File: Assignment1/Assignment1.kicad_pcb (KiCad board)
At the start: 2 copper layers, 50 x 50 mm, 22 parts, among them J1 Conn_01x02_Pin, J2 Conn_01x02_Pin, U1 TPS51386RJNR

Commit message: as1: momoi silkscreen and update bom
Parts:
- added G***: LOGO, momoi-n.preety:momoi-n, F.Cu at (58.5, 92.0)
- moved C8 13.5 mm to (89.5, 85.5)
- moved C3 9.00 mm to (80.5, 85.5)
- moved C2 4.50 mm to (76.0, 85.5)
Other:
- board text added: "NI__"
- board text added: "PCB Design Assignment 1"
- board text added: "Two-Stage Voltage Converter"

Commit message: add vias and copper zone as solid
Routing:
- net Earth: vias 8 -> 303
- added copper zone on F.Cu, net /Buck_SW

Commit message: Add silk screen for Vin, Vout and update track angle to 45
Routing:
- net /Buck_VBST: track 6.90 -> 6.32 mm
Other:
- board text added: "Vin"
- board text added: "Vout"
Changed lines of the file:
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@@
 		(layer "Edge.Cuts")
+	)
+	(gr_text "Vout\n"
+		(at 56.5 57 0)
+		(layer "F.Paste")
+		(effects
+			(font
+				(size 1 1)
+				(thickness 0.15)
+			)
+			(justify left bottom)
+		)
+	)
+	(gr_text "Vin"
+		(at 95 57.5 0)
+		(layer "F.Paste")
+		(effects
+			(font
+				(size 1 1)
+				(thickness 0.15)
+			)
+			(justify left bottom)
+		)
 	)
 	(gr_text "Two-Stage Voltage Converter"
@@
 	)
 	(segment
-		(start 94.525 76.975)
+		(start 94.525 75.975)
 		(end 94.525 75)
-		(width 0.3)
+		(width 0.35)
+		(layer "F.Cu")
+		(net 9)
+	)
+	(segment
+		(start 90.5 77)
+		(end 93.5 77)
+		(width 0.35)
 		(layer "F.Cu")
 		(net 9)
@@
 	)
 	(segment
-		(start 94.5 77)
-		(end 94.525 76.975)
-		(width 0.3)
+		(start 93.5 77)
+		(end 94.525 75.975)
+		(width 0.35)
 		(layer "F.Cu")
 		(net 9)
-	)
-	(segment
-		(start 90.5 77)
-		(end 94.5 77)
-		(width 0.3)
-		(layer "F.Cu")
-		(net 9)

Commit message: R1 C1 route
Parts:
- moved R1 2.17 mm to (94.5, 77.0)
- moved C1 1.28 mm to (94.5, 79.0)
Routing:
- net /Buck_VBST: track 6.32 -> 3.77 mm
- net Net-(C1-Pad1): track 4.16 -> 2.02 mm
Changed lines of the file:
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@@
 	(footprint "Capacitor_SMD:C_0603_1608Metric"
 		(layer "F.Cu")
-		(at 95.775 79 180)
+		(at 94.5 79 180)
 		(descr "Capacitor SMD 0603 (1608 Metric), square (rectangular) end terminal, IPC_7351 nominal, (Body size source: IPC-SM-782 page 76, https://www.pcb-3d.com/wordpress/wp-content/uploads/ipc-sm-782a_amendment_1_and_2.pdf), generated with kicad-footprint-generator")
 		(tags "capacitor")
@@
 	(footprint "Resistor_SMD:R_0603_1608Metric"
 		(layer "F.Cu")
-		(at 95.35 75)
+		(at 94.5 77)
 		(descr "Resistor SMD 0603 (1608 Metric), square (rectangular) end terminal, IPC_7351 nominal, (Body size source: IPC-SM-782 page 72, https://www.pcb-3d.com/wordpress/wp-content/uploads/ipc-sm-782a_amendment_1_and_2.pdf), generated with kicad-footprint-generator")
 		(tags "resistor")
@@
 	)
 	(segment
-		(start 96.55 75.55)
-		(end 96.55 79)
-		(width 0.3)
+		(start 95.325 78.95)
+		(end 95.275 79)
+		(width 1)
 		(layer "F.Cu")
 		(net 1)
 	)
 	(segment
-		(start 96.175 75)
-		(end 96.175 75.175)
-		(width 0.3)
+		(start 95.325 77)
+		(end 95.325 78.95)
+		(width 1)
 		(layer "F.Cu")
 		(net 1)
 	)
 	(segment
-		(start 96.175 75.175)
-		(end 96.55 75.55)
-		(width 0.3)
+		(start 93.725 79)
+		(end 92.5 79)
+		(width 1)
 		(layer "F.Cu")
-		(net 1)
+		(net 2)
 	)
 	(segment
@@
 	)
 	(segment
-		(start 93 78.5)
-		(end 90.5 78.5)
-		(width 0.3)
+		(start 92.5 79)
+		(end 92 78.5)
+		(width 1)
+		(layer "F.Cu")
+		(net 2)
+	)
+	(segment
+		(start 92 78.5)
+		(end 89.675 78.5)
+		(width 1)
 		(layer "F.Cu")
 		(net 2)
@@
 	)
 	(segment
-		(start 93.5 79)
-		(end 93 78.5)
-		(width 0.3)
-		(layer "F.Cu")
-		(net 2)
-	)
-	(segment
 		(start 89.875 77)
 		(end 89.875 75.775)
@@
 	)
 	(segment
-		(start 95 79)
-		(end 93.5 79)
-		(width 0.3)
-		(layer "F.Cu")
-		(net 2)
-	)
-	(segment
 		(start 90.5 73.5)
 		(end 90.4 73.6)
@@
 	)
 	(segment
+		(start 91.45 76.15)
+		(end 91.3 76)
+		(width 0.3)
+		(layer "F.Cu")
+		(net 7)
+	)
+	(segment
 		(start 94.675 71.5)
 		(end 94.675 70.325)
@@
 	)
 	(segment
-		(start 93.5 76)
-		(end 93.35 76.15)
+		(start 94.675 72.325)
+		(end 93.5 73.5)
 		(width 0.3)
 		(layer "F.Cu")
@@
 	)
 	(segment
-		(start 94.675 72.325)
-		(end 93.5 73.5)
+		(start 93.5 73.5)
+		(end 93.5 75.5)
 		(width 0.3)
 		(layer "F.Cu")
@@
 	)
 	(segment
-		(start 93.5 73.5)
-		(end 93.5 76)
+		(start 92.85 76.15)
+		(end 91.45 76.15)
 		(width 0.3)
 		(layer "F.Cu")
@@
 	)
 	(segment
-		(start 93.35 76.15)
-		(end 91.45 76.15)
-		(width 0.3)
-		(layer "F.Cu")
-		(net 7)
-	)
-	(segment
-		(start 91.45 76.15)
-		(end 91.3 76)
+		(start 93.5 75.5)
+		(end 92.85 76.15)
 		(width 0.3)
 		(layer "F.Cu")
@@
 	)
 	(segment
-		(start 90.4 76.9)
-		(end 90.5 77)
-		(width 0.3)
+		(start 91 77)
+		(end 93.675 77)
+		(width 0.5)
 		(layer "F.Cu")
 		(net 9)
 	)
 	(segment
-		(start 94.525 75.975)
-		(end 94.525 75)
-		(width 0.35)
+		(start 90.4 76.15)
+		(end 90.4 76.4)
+		(width 0.3)
 		(layer "F.Cu")
 		(net 9)
 	)
 	(segment
-		(start 90.5 77)
-		(end 93.5 77)
-		(width 0.35)
+		(start 90.5 76.5)
+		(end 91 77)
+		(width 0.5)
 		(layer "F.Cu")
 		(net 9)
 	)
 	(segment
-		(start 90.4 76.15)
-		(end 90.4 76.9)
+		(start 90.4 76.4)
+		(end 90.5 76.5)
 		(width 0.3)
 		(layer "F.Cu")
 		(net 9)
-	)
-	(segment
-		(start 93.5 77)
-		(end 94.525 75.975)
-		(width 0.35)
-		(layer "F.Cu")
-		(net 9)

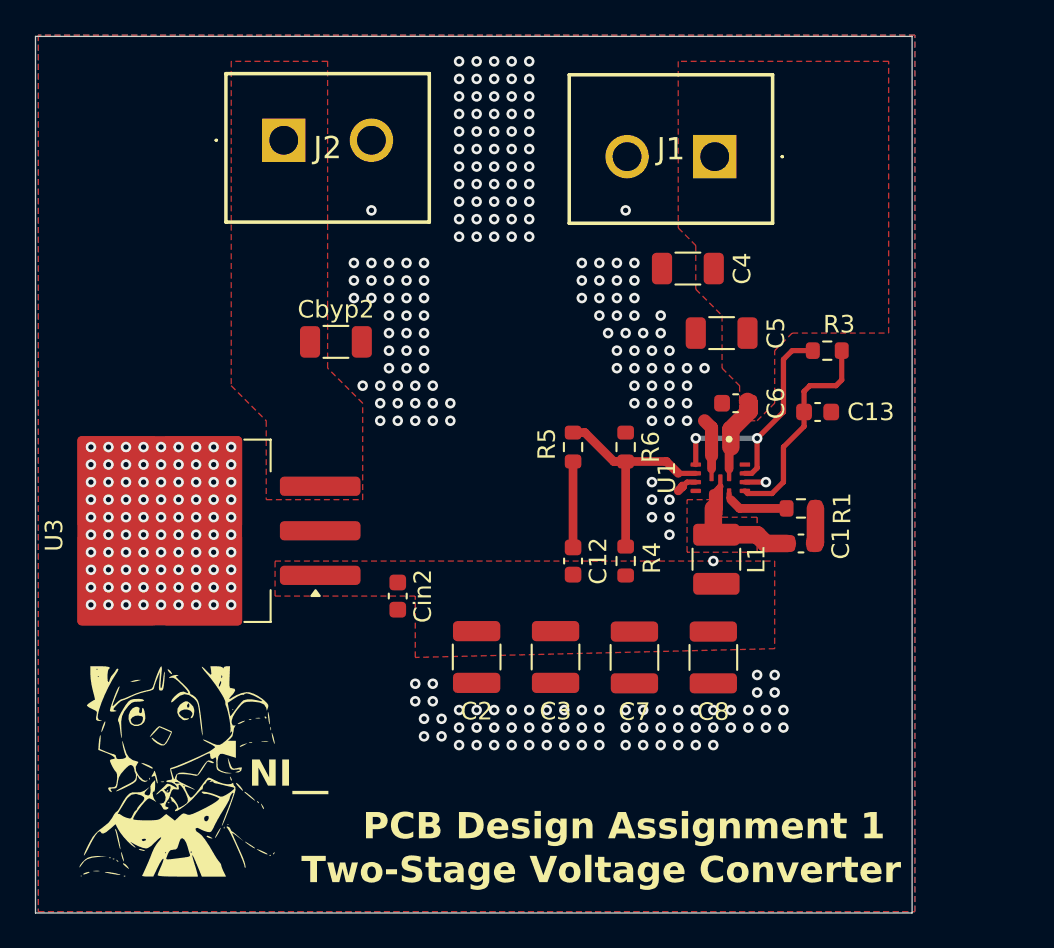
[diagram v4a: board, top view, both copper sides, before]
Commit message: make LDO copper plane solid
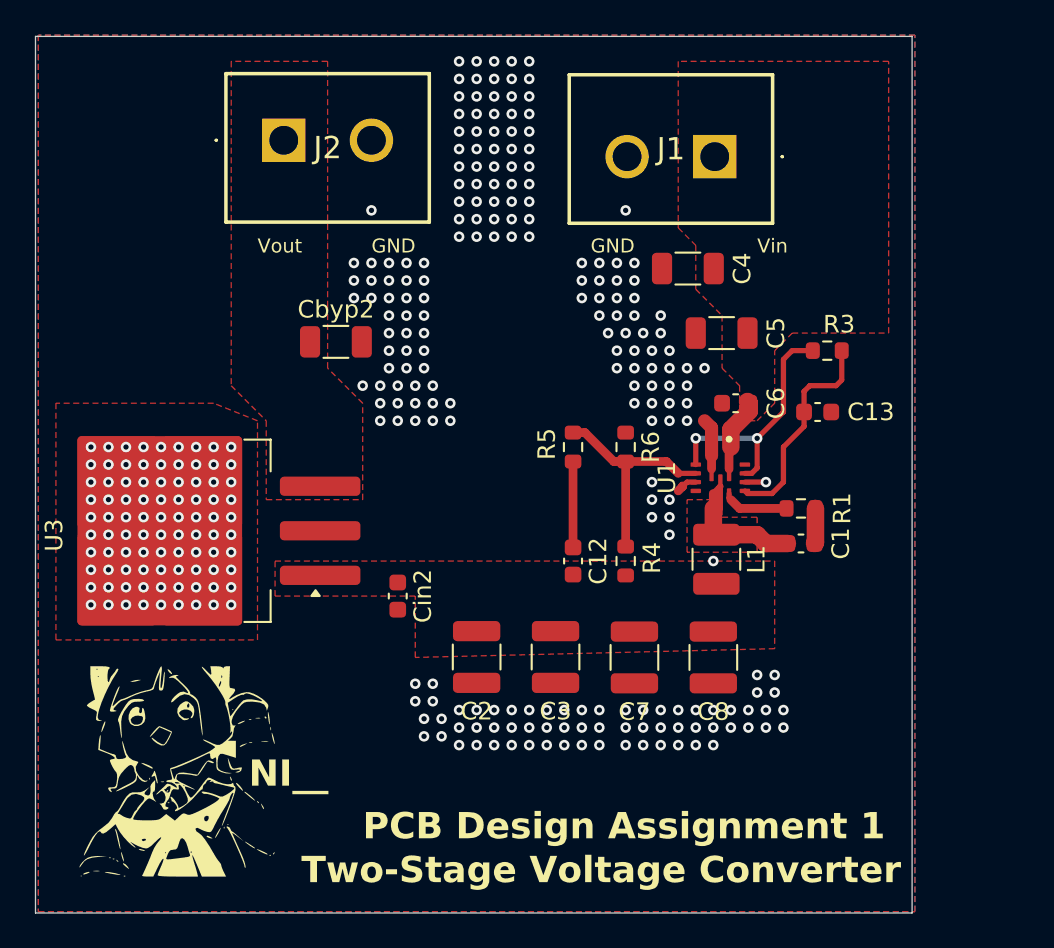
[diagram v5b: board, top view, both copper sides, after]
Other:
- board text added: "GND"
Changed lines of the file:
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@@
 		(layer "Edge.Cuts")
-	)
-	(gr_text "Vout\n"
-		(at 56.5 57 0)
-		(layer "F.Paste")
-		(effects
-			(font
-				(size 1 1)
-				(thickness 0.15)
-			)
-			(justify left bottom)
-		)
-	)
-	(gr_text "Vin"
-		(at 95 57.5 0)
-		(layer "F.Paste")
-		(effects
-			(font
-				(size 1 1)
-				(thickness 0.15)
-			)
-			(justify left bottom)
-		)
 	)
 	(gr_text "Two-Stage Voltage Converter"
@@
 		)
 	)
+	(gr_text "GND"
+		(at 70 62.5 0)
+		(layer "F.SilkS")
+		(effects
+			(font
+				(size 0.8 0.8)
+				(thickness 0.125)
+			)
+			(justify left bottom)
+		)
+	)
+	(gr_text "GND"
+		(at 82.5 62.5 0)
+		(layer "F.SilkS")
+		(effects
+			(font
+				(size 0.8 0.8)
+				(thickness 0.125)
+			)
+			(justify left bottom)
+		)
+	)
+	(gr_text "Vout\n"
+		(at 63.5 62.5 0)
+		(layer "F.SilkS")
+		(effects
+			(font
+				(size 0.8 0.8)
+				(thickness 0.125)
+			)
+			(justify left bottom)
+		)
+	)
 	(gr_text "NI__"
 		(at 63 93 0)
@@
 				(thickness 0.3)
 				(bold yes)
+			)
+			(justify left bottom)
+		)
+	)
+	(gr_text "Vin"
+		(at 92 62.5 0)
+		(layer "F.SilkS")
+		(effects
+			(font
+				(size 0.8 0.8)
+				(thickness 0.125)
 			)
 			(justify left bottom)
@@
 			)
 		)
+	)
+	(zone
+		(net 4)
+		(net_name "Earth")
+		(layer "F.Cu")
+		(hatch edge 0.5)
+		(priority 6)
+		(connect_pads yes
+			(clearance 0.3)
+		)
+		(min_thickness 0.25)
+		(filled_areas_thickness no)
+		(fill yes
+			(thermal_gap 0.5)
+			(thermal_bridge_width 0.5)
+		)
+		(polygon
+			(pts
+				(xy 63.5 84.5) (xy 63.5 72) (xy 61 71) (xy 52 71) (xy 52 84.5)
+			)
+		)
